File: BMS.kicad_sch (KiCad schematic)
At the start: 57 parts, among them Q1 BD140, Q10 IRF4905, Q11 IRF4905, Q2 BD140, Q3 BD140, Q6 IRF4905, Q7 IRF4905, Q8 IRF4905, Q9 IRF4905, T1 Transformer_1P_1S, U1 TL431DBZ, U2 LM317L_SOT-89, U3 LM317L_SOT-89, U4 TL431DBZ, U5 TL431DBZ, U7 DW01A, U8 DW01A, U9 DW01A

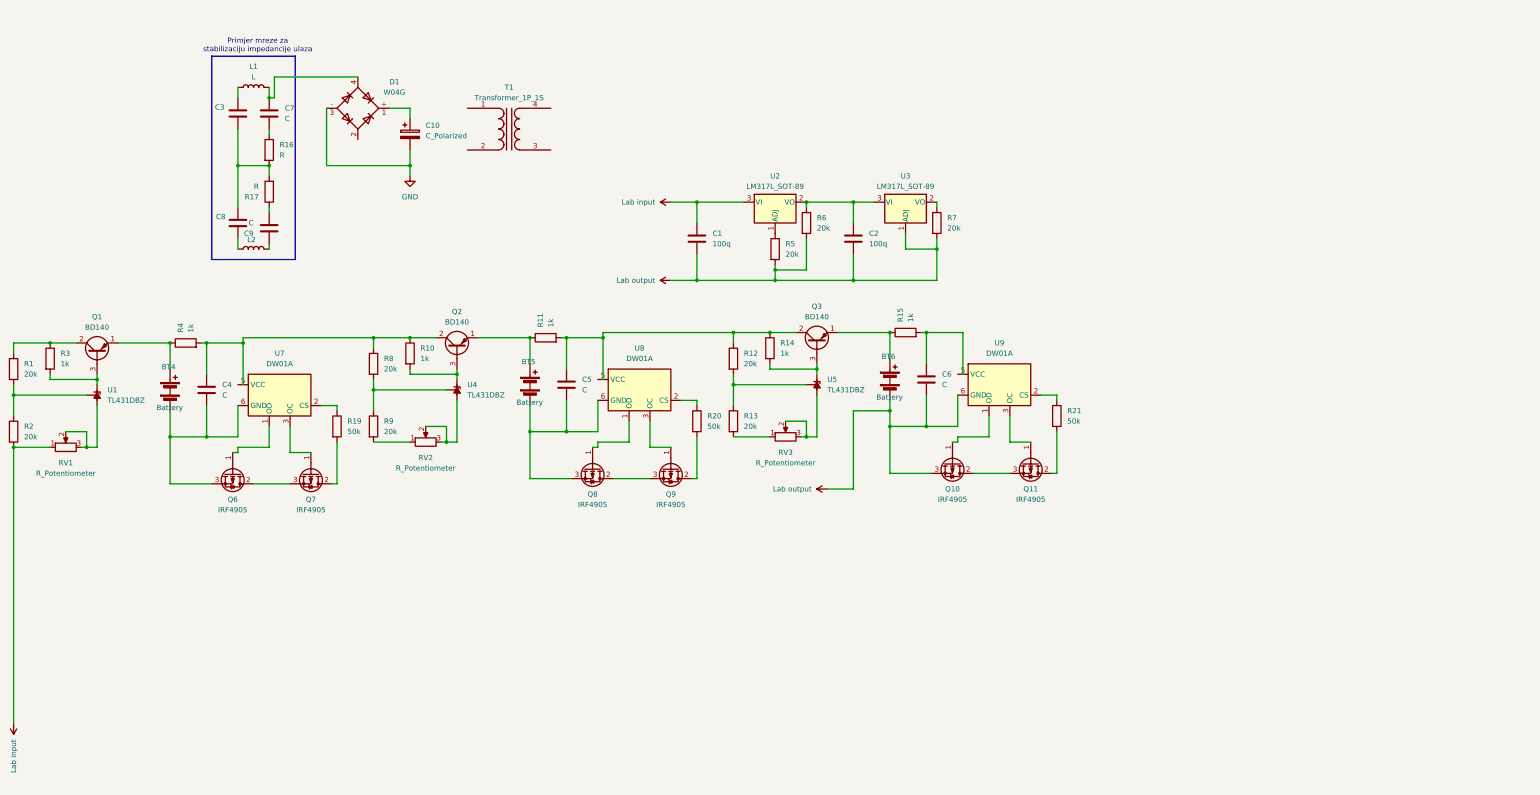
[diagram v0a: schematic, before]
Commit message: Lecture Update
Updated some forms in charging section
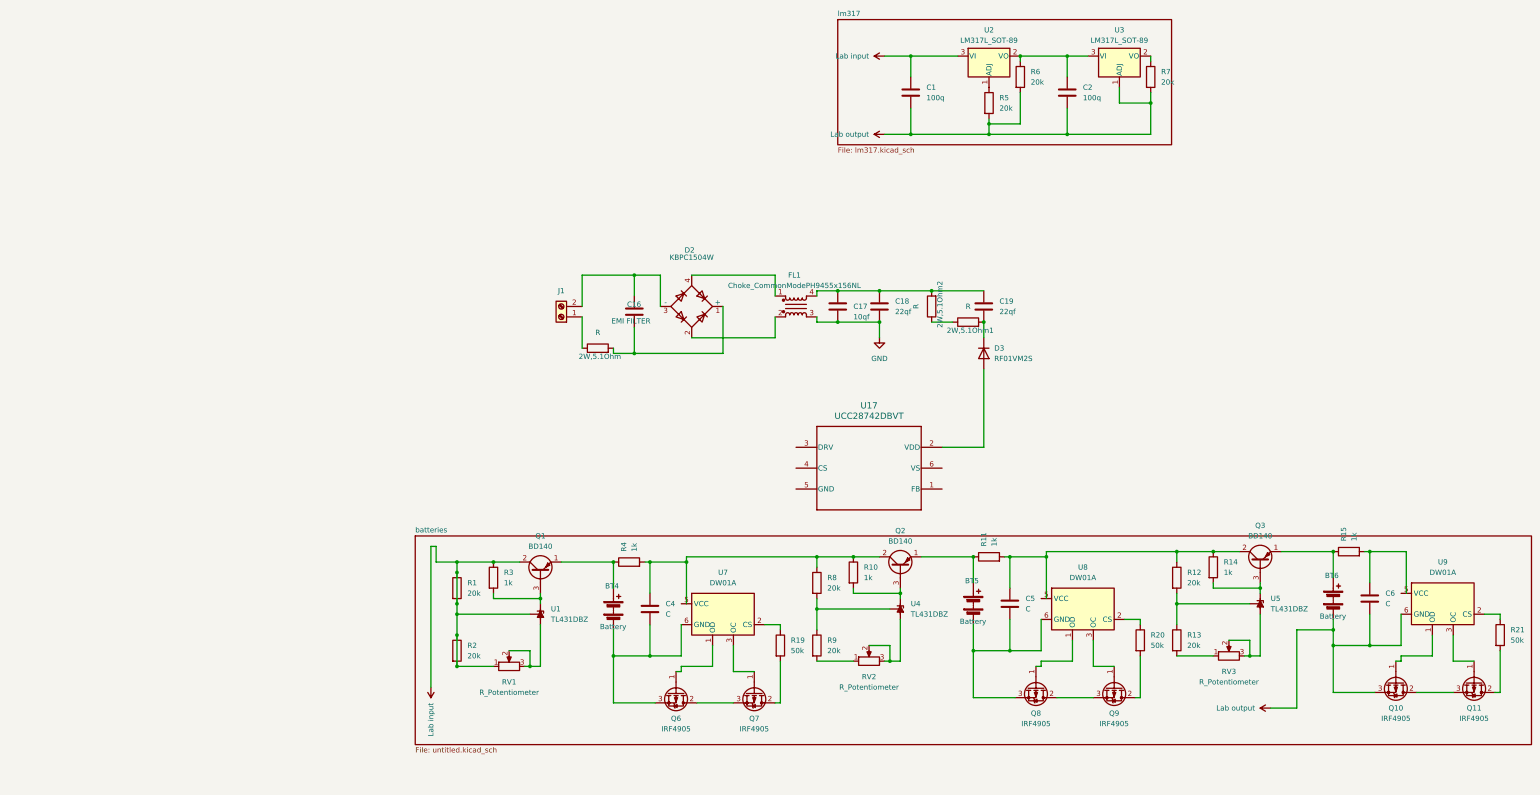
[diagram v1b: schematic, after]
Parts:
- removed C10: C_Polarized, symbol Device:C_Polarized
- removed C3, C7, C8, C9: C, symbol Device:C
- removed D1: W04G, Diode_THT:Diode_Bridge_Round_D9.8mm, symbol Diode_Bridge:W04G
- removed L1, L2: L, symbol Device:L
- removed R16, R17: R, symbol Device:R
- removed T1: Transformer_1P_1S, symbol Device:Transformer_1P_1S
- added 2W,5.1Ohm, 2W,5.1Ohm1, 2W,5.1Ohm2: R, Resistor_THT:R_Axial_DIN0414_L11.9mm_D4.5mm_P15.24mm_Horizontal, symbol Device:R
- added C16: EMI FILTER, symbol Device:C
- added C17: 10qf, Capacitor_THT:CP_Radial_D5.0mm_P2.00mm, symbol Device:C
- added C18, C19: 22qf, Capacitor_THT:CP_Radial_D5.0mm_P2.00mm, symbol Device:C
- added D2: KBPC1504W, Diode_THT:Diode_Bridge_GeneSiC_KBPC_W, symbol Diode_Bridge:KBPC1504W
- added D3: RF01VM2S, Diode_SMD:D_SOD-323, symbol Diode:RF01VM2S
- added FL1: Choke_CommonModePH9455x156NL, Inductor_THT:L_CommonMode_PulseElectronics_PH9455xxx6NL_2, symbol Filter:Choke_CommonMode_PulseElectronics_PH9455x156NL
- added J1: Screw_Terminal_01x02, symbol Connector:Screw_Terminal_01x02
- added U17: UCC28742DBVT, DBV0006A_N, symbol UCC28742:UCC28742DBVT
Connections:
- net GND: now also C17.2, C18.2, FL1.3
- net Lab input: now also Q1.2 (C), R1.1, R1.2, R2.1, R3.1, U1.2 (REF)
- new net: 2W,5.1Ohm1.2, C19.2, D3.1 (K)
- new net: D3.2 (A), U17.2 (VDD)
- new net: 2W,5.1Ohm.2, C16.2, D2.1 (+)
- new net: D2.2, FL1.2
- new net: C16.1, D2.3 (-), J1.2 (Pin_2)
- new net: D2.4, FL1.1
- new net: 2W,5.1Ohm1.1, 2W,5.1Ohm2.1
- new net: 2W,5.1Ohm.1, J1.1 (Pin_1)
- new net: 2W,5.1Ohm2.2, C17.1, C18.1, C19.1, FL1.4
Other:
- added sheet batteries (untitled.kicad_sch)
- added sheet lm317 (lm317.kicad_sch)
- note removed: "Primjer mreze za stabilizaciju impedancije ulaza"
- moved on the sheet: BT4, BT5, BT6, C1, C2, C4, C5, C6, Q1, Q10, Q11, Q2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

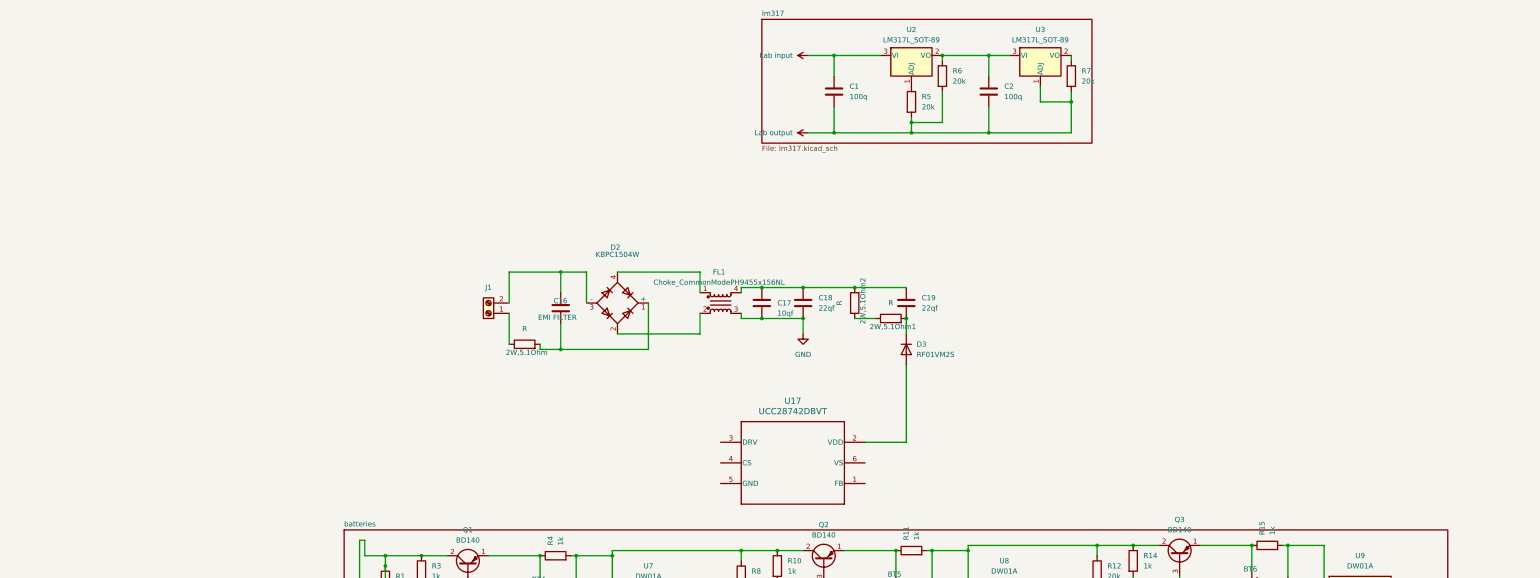
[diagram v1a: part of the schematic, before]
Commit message: ac dc converter set with flyback transformer
Preparation for 5V with 12V headers
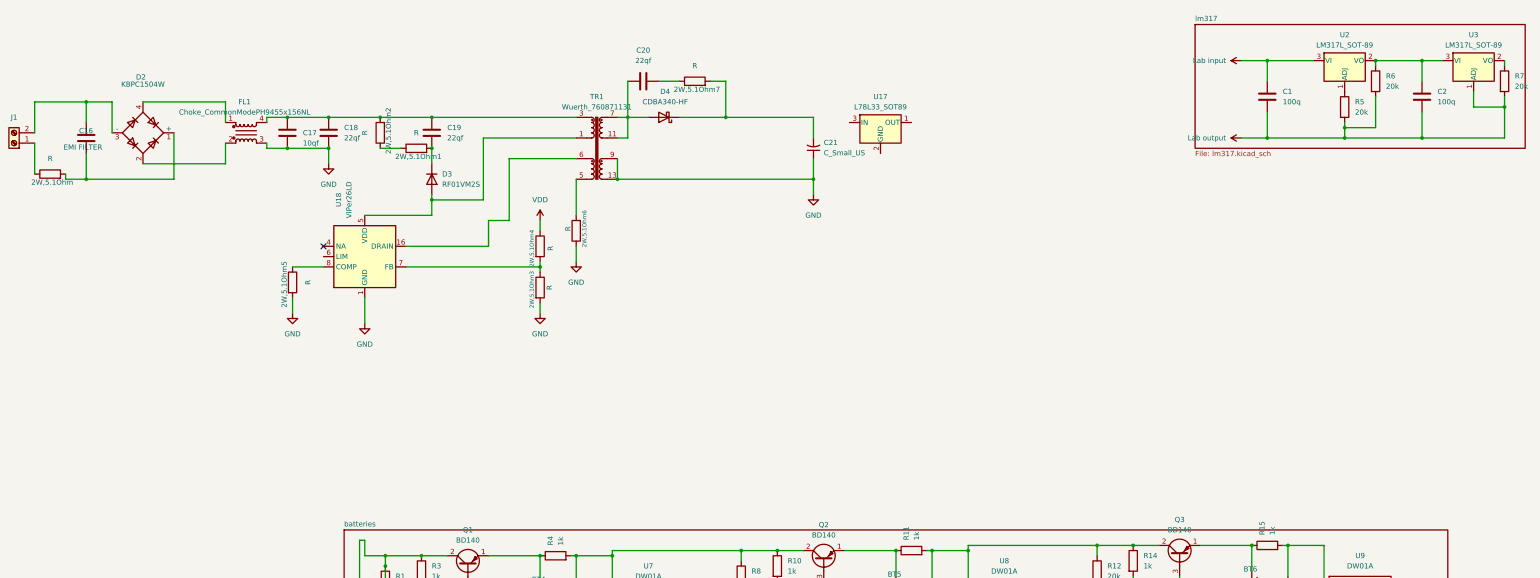
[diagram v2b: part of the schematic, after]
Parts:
- removed U17: UCC28742DBVT, DBV0006A_N, symbol UCC28742:UCC28742DBVT
- added 2W,5.1Ohm3, 2W,5.1Ohm4, 2W,5.1Ohm5, 2W,5.1Ohm6, 2W,5.1Ohm7: R, Resistor_THT:R_Axial_DIN0414_L11.9mm_D4.5mm_P15.24mm_Horizontal, symbol Device:R
- added C20: 22qf, Capacitor_THT:CP_Radial_D5.0mm_P2.00mm, symbol Device:C
- added C21: C_Small_US, symbol Device:C_Small_US
- added D4: CDBA340-HF, Diode_SMD:D_SMA, symbol Diode:CDBA340-HF
- added TR1: Wuerth_760871131, Transformer_THT:Transformer_Wuerth_760871131, symbol Transformer:Wuerth_760871131
- added U17: L78L33_SOT89, Package_TO_SOT_SMD:SOT-89-3, symbol Regulator_Linear:L78L33_SOT89
- added U18: VIPer26LD, Package_SO:SOIC-16_3.9x9.9mm_P1.27mm, symbol Regulator_Switching:VIPer26LD
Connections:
- net GND: now also 2W,5.1Ohm3.2, 2W,5.1Ohm5.2, 2W,5.1Ohm6.1, C21.1, TR1.10, TR1.13, TR1.14, TR1.9, U18.1 (GND), U18.2 (GND)
- net at D3.2 (A): now also TR1.1, U18.5 (VDD)
- net at 2W,5.1Ohm2.2, C17.1, C18.1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: now also TR1.3
- new net: 2W,5.1Ohm6.2, TR1.5
- new net: 2W,5.1Ohm7.1, C20.2
- new net: 2W,5.1Ohm7.2, C21.2, D4.1 (K)
- new net: 2W,5.1Ohm5.1, U18.8 (COMP)
- new net: C20.1, D4.2 (A), TR1.11, TR1.12, TR1.7, TR1.8
- new net: TR1.6, U18.13 (DRAIN), U18.14 (DRAIN), U18.15 (DRAIN), U18.16 (DRAIN)
- new net: 2W,5.1Ohm3.1, 2W,5.1Ohm4.2, U18.7 (FB)
- new net VDD: 2W,5.1Ohm4.1
- no-connect marks 0 -> 1
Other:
- moved on the sheet: 2W,5.1Ohm, 2W,5.1Ohm1, 2W,5.1Ohm2, C1, C16, C17, C18, C19, C2, D2, D3, FL1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

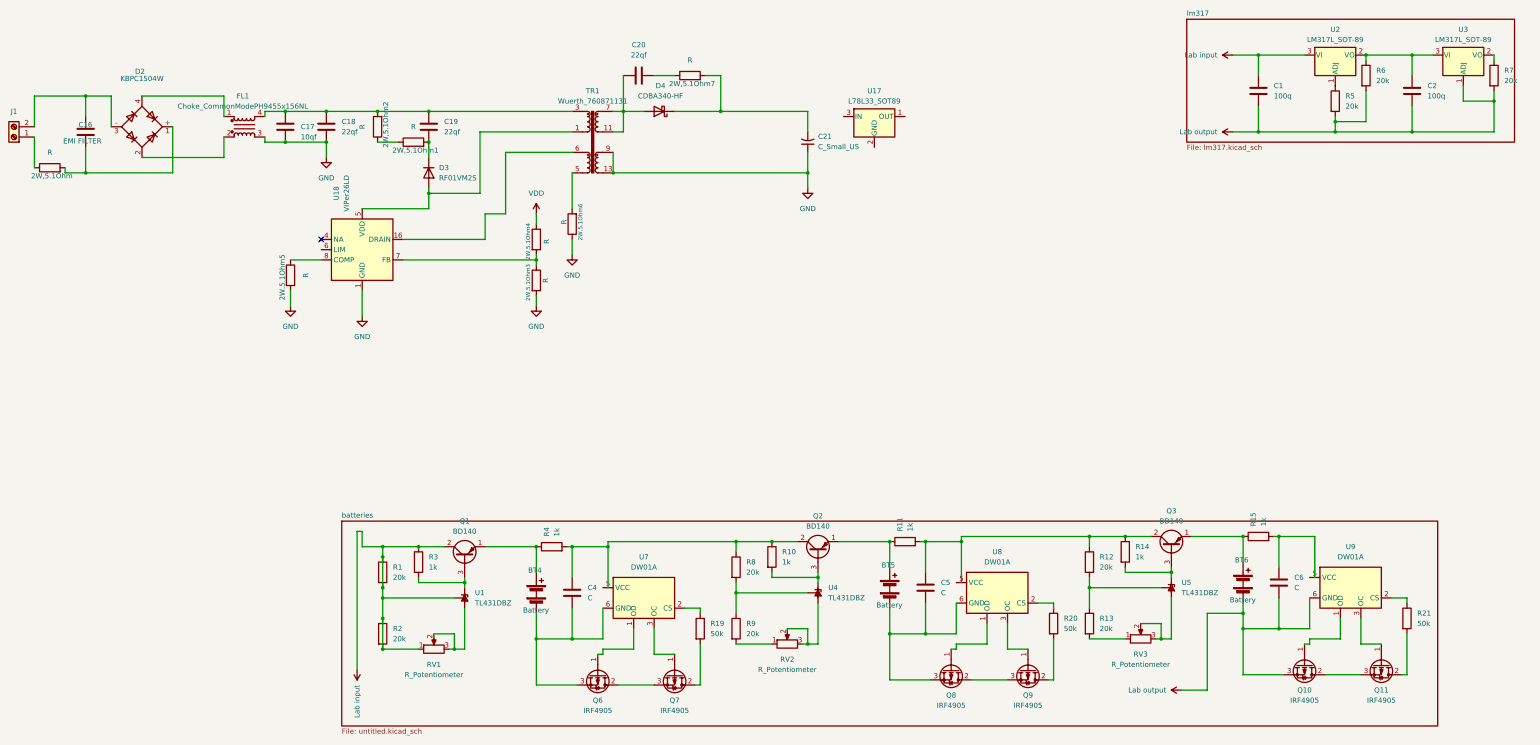
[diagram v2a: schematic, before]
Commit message: flyback transformer
Flyback transformer fixed along with regulation
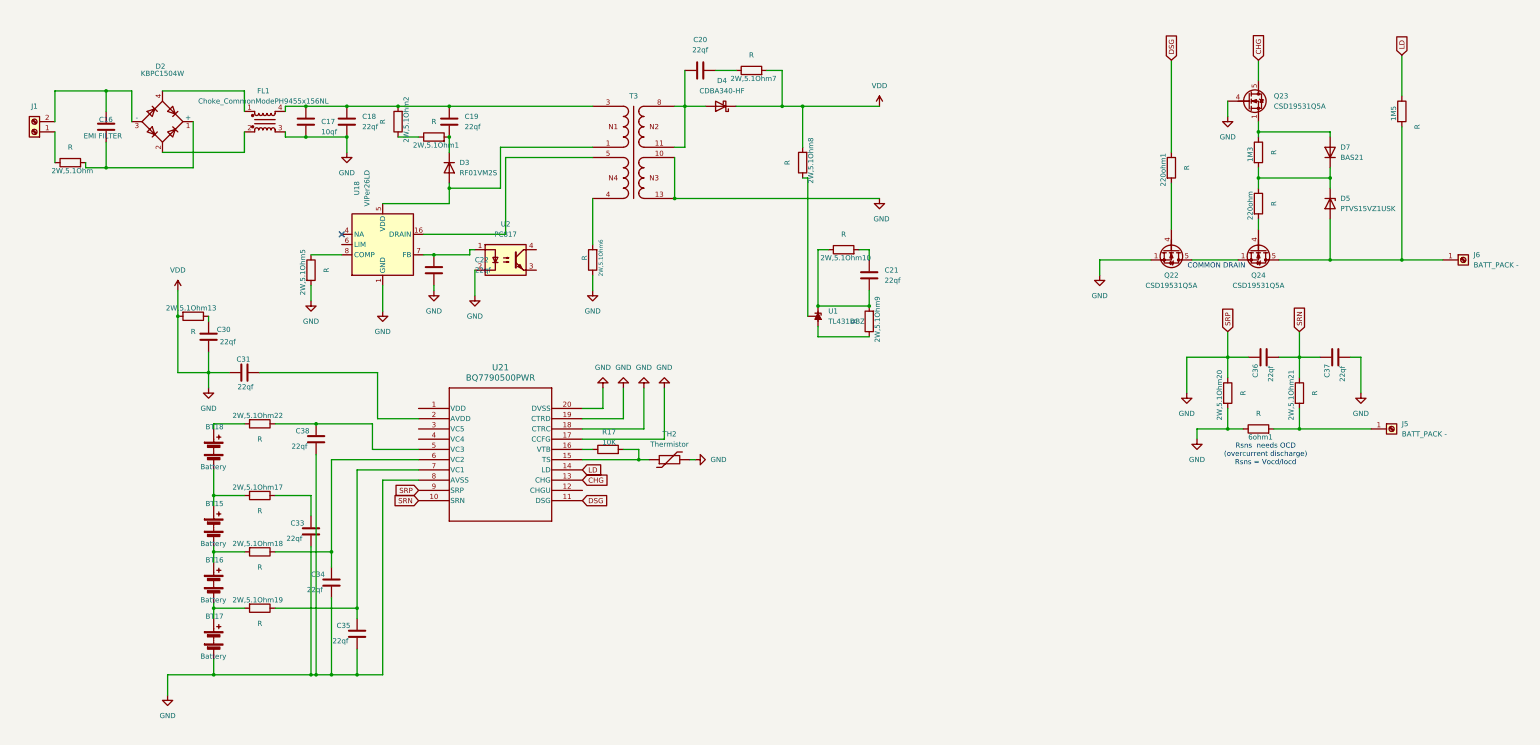
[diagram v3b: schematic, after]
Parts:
- removed 2W,5.1Ohm3, 2W,5.1Ohm4: R, Resistor_THT:R_Axial_DIN0414_L11.9mm_D4.5mm_P15.24mm_Horizontal, symbol Device:R
- removed BT4, BT5, BT6: Battery, symbol Device:Battery
- removed C1, C2: 100q, Capacitor_SMD:C_0805_2012Metric, symbol Device:C
- removed C21: C_Small_US, symbol Device:C_Small_US
- removed C4, C5, C6: C, symbol Device:C
- removed Q1, Q2, Q3: BD140, Package_TO_SOT_THT:TO-126-3_Vertical, symbol Transistor_BJT:BD140
- removed Q10, Q11, Q6, Q7, Q8, Q9: IRF4905, Package_TO_SOT_THT:TO-220-3_Vertical, symbol Transistor_FET:IRF4905
- removed R1, R12, R13, R2, R8, R9: 20k, Resistor_SMD:R_0612_1632Metric_Pad1.18x3.40mm_HandSolder, symbol Device:R
- removed R10, R11, R14, R15, R3, R4: 1k, Resistor_SMD:R_0612_1632Metric_Pad1.18x3.40mm_HandSolder, symbol Device:R
- removed R19, R20, R21: 50k, Resistor_SMD:R_0612_1632Metric_Pad1.18x3.40mm_HandSolder, symbol Device:R
- removed R5, R6, R7: 20k, Resistor_SMD:R_0805_2012Metric, symbol Device:R
- removed RV1, RV2, RV3: R_Potentiometer, symbol Device:R_Potentiometer
- removed TR1: Wuerth_760871131, Transformer_THT:Transformer_Wuerth_760871131, symbol Transformer:Wuerth_760871131
- removed U17: L78L33_SOT89, Package_TO_SOT_SMD:SOT-89-3, symbol Regulator_Linear:L78L33_SOT89
- removed U2, U3: LM317L_SOT-89, Package_TO_SOT_SMD:SOT-89-3, symbol Regulator_Linear:LM317L_SOT-89
- removed U4, U5: TL431DBZ, Package_TO_SOT_SMD:SOT-23, symbol Reference_Voltage:TL431DBZ
- removed U7, U8, U9: DW01A, Package_TO_SOT_SMD:SOT-23-6, symbol Battery_Management:DW01A
- added 1M3, 1M5, 220ohm, 220ohm1, 2W,5.1Ohm10, 2W,5.1Ohm13, 2W,5.1Ohm17, 2W,5.1Ohm18, 2W,5.1Ohm19, 2W,5.1Ohm20, 2W,5.1Ohm21, 2W,5.1Ohm22, 2W,5.1Ohm8, 2W,5.1Ohm9, 6ohm1: R, Resistor_THT:R_Axial_DIN0414_L11.9mm_D4.5mm_P15.24mm_Horizontal, symbol Device:R
- added BT15, BT16, BT17, BT18: Battery, symbol Device:Battery
- added C21, C22, C30, C31, C33, C34, C35, C36, C37, C38: 22qf, Capacitor_THT:CP_Radial_D5.0mm_P2.00mm, symbol Device:C
- added D5: PTVS15VZ1USK, Diode_SMD:Nexperia_DSN1608-2_1.6x0.8mm, symbol Diode:PTVS15VZ1USK
- added D7: BAS21, Package_TO_SOT_SMD:SOT-23, symbol Diode:BAS21
- added J5, J6: BATT_PACK -, symbol Connector:Screw_Terminal_01x01
- added Q22, Q23, Q24: CSD19531Q5A, Package_TO_SOT_SMD:TDSON-8-1, symbol Transistor_FET:CSD19531Q5A
- added R17: 10K, Resistor_SMD:R_0805_2012Metric, symbol Device:R
- added T3: EE20_10_6_750811647, Transformer_THT_Wurth:T_Wurth_WE-OLTI-EE20_10_6_750811647, symbol WURTHTransformator:EE20_10_6_750811647
- added TH2: Thermistor, symbol Device:Thermistor
- added U2: PC817, Package_DIP:DIP-4_W7.62mm, symbol Isolator:PC817
- added U21: BQ7790500PWR, PW20_TEX, symbol BQ77905:BQ7790500PWR
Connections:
- net GND: now also 2W,5.1Ohm7.2, D4.1 (K), 2W,5.1Ohm13.2, 2W,5.1Ohm20.1, 2W,5.1Ohm20.2, 2W,5.1Ohm8.2, 6ohm1.1, BT17.2 (-), C22.2, C30.1, C31.1, C33.1, C34.1, C35.1, C36.2, C37.1, C38.1, Q22.1 (S), Q22.2 (S), Q22.3 (S), Q23.4 (G), T3.10, T3.13, TH2.2, U2.2, U21.17 (CCFG), U21.18 (CTRC), U21.19 (CTRD), U21.20 (DVSS), U21.8 (AVSS), U21.9 (SRP)
- net at D3.2 (A), U18.5 (VDD): now also T3.1
- net at 2W,5.1Ohm6.2: now also T3.4
- net at C20.1, D4.2 (A): now also T3.11, T3.8
- net at U1.1 (K): now also 2W,5.1Ohm10.1, 2W,5.1Ohm9.2, C21.1
- net at 2W,5.1Ohm2.2, C17.1, C18.1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: now also T3.3
- net at U18.13 (DRAIN), U18.14 (DRAIN), U18.15 (DRAIN)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: now also T3.5
- net at U18.7 (FB): now also C22.1, U2.1
- net at U1.3 (A): now also 2W,5.1Ohm9.1
- net Lab input: no longer names the net of U1.2 (REF)
- net Lab input: now also 2W,5.1Ohm8.1
- new net: R17.2, TH2.1, U21.15 (TS)
- new net: 2W,5.1Ohm21.2, 6ohm1.2, J5.1 (Pin_1)
- new net: 1M5.2, D5.2 (A), J6.1 (Pin_1), Q24.5 (D)
- new net: 2W,5.1Ohm17.1, C33.2
- new net: 2W,5.1Ohm17.2, BT15.1 (+), BT18.2 (-)
- new net: 220ohm1.2, Q22.4 (G)
- new net: 1M3.1, D7.1 (A), Q23.1 (S), Q23.2 (S), Q23.3 (S)
- new net: 2W,5.1Ohm10.2, C21.2
- new net: 1M3.2, 220ohm.1, D5.1 (K), D7.3 (K)
- new net: 2W,5.1Ohm19.2, BT16.2 (-), BT17.1 (+)
- new net: 2W,5.1Ohm18.2, BT15.2 (-), BT16.1 (+)
- new net: Q22.5 (D), Q24.1 (S), Q24.2 (S), Q24.3 (S)
- new net: 2W,5.1Ohm19.1, C35.2, U21.7 (VC1)
- new net: 2W,5.1Ohm13.1, C30.2
- new net: 2W,5.1Ohm22.1, C38.2, U21.5 (VC3)
- new net: 220ohm.2, Q24.4 (G)
- new net: C31.2, U21.2 (AVDD)
- new net: R17.1, U21.16 (VTB)
- new net: 2W,5.1Ohm18.1, C34.2, U21.6 (VC2)
- new net: 2W,5.1Ohm22.2, BT18.1 (+)
- new net CHG: Q23.5 (D), U21.13 (CHG)
- new net DSG: 220ohm1.1, U21.11 (DSG)
- new net LD: 1M5.1, U21.14 (LD)
- new net SRN: 2W,5.1Ohm21.1, C36.1, C37.2, U21.10 (SRN)
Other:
- removed sheet batteries
- removed sheet lm317
- note added: "COMMON DRAIN"
- note added: "Rsns needs OCD (overcurrent discharge) Rsns = Vocd/Iocd"
- moved on the sheet: 2W,5.1Ohm, 2W,5.1Ohm1, 2W,5.1Ohm2, 2W,5.1Ohm5, 2W,5.1Ohm6, 2W,5.1Ohm7, C16, C17, C18, C19, C20, D2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
